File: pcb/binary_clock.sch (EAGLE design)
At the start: 18 parts

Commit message: PCB almost done.
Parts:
- added C1: (no value), rcl:C-EUC0603K
- added R1, R2: (no value), rcl:R-EU_R0603
- added S1: SET, SparkFun-Switches:MOMENTARY-SWITCH-SPST-SMD-5.2-REDUNDANT
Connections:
- new net LED_CK: R1.1, U$1.(OCP)PB1
- new net LED_D: R2.1, U$1.(AREF)PB0
- new net N$31: D17.DO
- new net N$32: U$1.(ADC0)PB5
- new net N$33: U$1.(ADC2)PB4
- new net N$34: D17.CO
- new net N$35: U$1.(ADC3)PB3
- new net N$36: U$1.(ADC1)PB2
- new net N$41: D1.DI, R2.2
- new net N$42: D1.CI, R1.2
- new net SW: S1.1
- net +5V: now also C1.1
- net GND: now also C1.2, S1.2
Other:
- moved on the sheet: D1, D10, D11, D2, D3, D4, D5, D6, D7, D8, D9, U$1

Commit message: Switch connected
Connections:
- removed net N$36: U$1.(ADC1)PB2
- net SW: now also U$1.(ADC1)PB2
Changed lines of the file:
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@@
-</segment>
-</net>
-<net name="N$36" class="0">
-<segment>
-<pinref part="U$1" gate="G$1" pin="(ADC1)PB2"/>
-<wire x1="-12.7" y1="71.12" x2="-10.16" y2="71.12" width="0.1524" layer="91"/>
 </segment>
 </net>
@@
 <label x="17.78" y="60.96" size="0.8128" layer="95" rot="R180" xref="yes"/>
 </segment>
+<segment>
+<pinref part="U$1" gate="G$1" pin="(ADC1)PB2"/>
+<wire x1="-12.7" y1="71.12" x2="-10.16" y2="71.12" width="0.1524" layer="91"/>
+<label x="-10.16" y="71.12" size="0.8128" layer="95" xref="yes"/>
+</segment>
 </net>

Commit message: Routing done.
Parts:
- added R3: (no value), rcl:R-EU_R0603
- added Y1: OSCILLATORSMD-5X3, SparkFun-Clocks:OSCILLATORSMD-5X3
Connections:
- new net N$36: R3.2, S1.1
- net +5V: now also Y1.VCC
- net GND: now also Y1.GND
- net N$35: now also Y1.OUT
- net SW: now also R3.1; no longer S1.1
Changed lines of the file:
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@@
 <?xml version="1.0" encoding="utf-8"?>
 <!DOCTYPE eagle SYSTEM "eagle.dtd">
-<eagle version="7.6.0">
+<eagle version="7.7.0">
 <drawing>
 <settings>
@@
 <layers>
 <layer number="1" name="Top" color="4" fill="1" visible="no" active="no"/>
+<layer number="2" name="Route2" color="1" fill="3" visible="no" active="no"/>
+<layer number="3" name="Route3" color="4" fill="3" visible="no" active="no"/>
+<layer number="4" name="Route4" color="1" fill="4" visible="no" active="no"/>
+<layer number="5" name="Route5" color="4" fill="4" visible="no" active="no"/>
+<layer number="6" name="Route6" color="1" fill="8" visible="no" active="no"/>
+<layer number="7" name="Route7" color="4" fill="8" visible="no" active="no"/>
+<layer number="8" name="Route8" color="1" fill="2" visible="no" active="no"/>
+<layer number="9" name="Route9" color="4" fill="2" visible="no" active="no"/>
+<layer number="10" name="Route10" color="1" fill="7" visible="no" active="no"/>
+<layer number="11" name="Route11" color="4" fill="7" visible="no" active="no"/>
+<layer number="12" name="Route12" color="1" fill="5" visible="no" active="no"/>
+<layer number="13" name="Route13" color="4" fill="5" visible="no" active="no"/>
+<layer number="14" name="Route14" color="1" fill="6" visible="no" active="no"/>
+<layer number="15" name="Route15" color="4" fill="6" visible="no" active="no"/>
 <layer number="16" name="Bottom" color="1" fill="1" visible="no" active="no"/>
 <layer number="17" name="Pads" color="2" fill="1" visible="no" active="no"/>
@@
 <part name="R1" library="rcl" deviceset="R-EU_" device="R0603"/>
 <part name="R2" library="rcl" deviceset="R-EU_" device="R0603"/>
+<part name="Y1" library="SparkFun-Clocks" deviceset="OSCILLATOR" device="SMD-5X3"/>
+<part name="R3" library="rcl" deviceset="R-EU_" device="R0603"/>
 </parts>
 <sheets>
@@
 <instance part="R1" gate="G$1" x="33.02" y="76.2"/>
 <instance part="R2" gate="G$1" x="33.02" y="73.66"/>
+<instance part="Y1" gate="G$1" x="-30.48" y="96.52"/>
+<instance part="R3" gate="G$1" x="12.7" y="60.96"/>
 </instances>
 <busses>
@@
 <label x="-53.34" y="33.02" size="0.8128" layer="95" rot="R180" xref="yes"/>
 </segment>
+<segment>
+<pinref part="Y1" gate="G$1" pin="GND"/>
+<wire x1="-20.32" y1="93.98" x2="-17.78" y2="93.98" width="0.1524" layer="91"/>
+</segment>
 </net>
 <net name="+5V" class="0">
@@
 <wire x1="-53.34" y1="43.18" x2="-53.34" y2="45.72" width="0.1524" layer="91"/>
 <label x="-53.34" y="45.72" size="0.8128" layer="95" rot="R180" xref="yes"/>
+</segment>
+<segment>
+<pinref part="Y1" gate="G$1" pin="VCC"/>
+<wire x1="-40.64" y1="99.06" x2="-43.18" y2="99.06" width="0.1524" layer="91"/>
 </segment>
 </net>
@@
 <segment>
 <pinref part="U$1" gate="G$1" pin="(ADC3)PB3"/>
-<wire x1="-12.7" y1="73.66" x2="-10.16" y2="73.66" width="0.1524" layer="91"/>
+<pinref part="Y1" gate="G$1" pin="OUT"/>
+<wire x1="-20.32" y1="99.06" x2="2.54" y2="99.06" width="0.1524" layer="91"/>
+<wire x1="2.54" y1="99.06" x2="2.54" y2="73.66" width="0.1524" layer="91"/>
+<wire x1="2.54" y1="73.66" x2="-12.7" y2="73.66" width="0.1524" layer="91"/>
 </segment>
 </net>
@@
 <net name="SW" class="0">
 <segment>
-<pinref part="S1" gate="G$1" pin="1"/>
-<wire x1="20.32" y1="60.96" x2="17.78" y2="60.96" width="0.1524" layer="91"/>
-<label x="17.78" y="60.96" size="0.8128" layer="95" rot="R180" xref="yes"/>
-</segment>
-<segment>
 <pinref part="U$1" gate="G$1" pin="(ADC1)PB2"/>
 <wire x1="-12.7" y1="71.12" x2="-10.16" y2="71.12" width="0.1524" layer="91"/>
 <label x="-10.16" y="71.12" size="0.8128" layer="95" xref="yes"/>
 </segment>
-</net>
+<segment>
+<pinref part="R3" gate="G$1" pin="1"/>
+<wire x1="7.62" y1="60.96" x2="5.08" y2="60.96" width="0.1524" layer="91"/>
+<label x="5.08" y="60.96" size="0.8128" layer="95" rot="R180" xref="yes"/>
+</segment>
+</net>
+<net name="N$36" class="0">
+<segment>
+<pinref part="S1" gate="G$1" pin="1"/>
+<pinref part="R3" gate="G$1" pin="2"/>
+<wire x1="17.78" y1="60.96" x2="20.32" y2="60.96" width="0.1524" layer="91"/>
+</segment>
+</net>

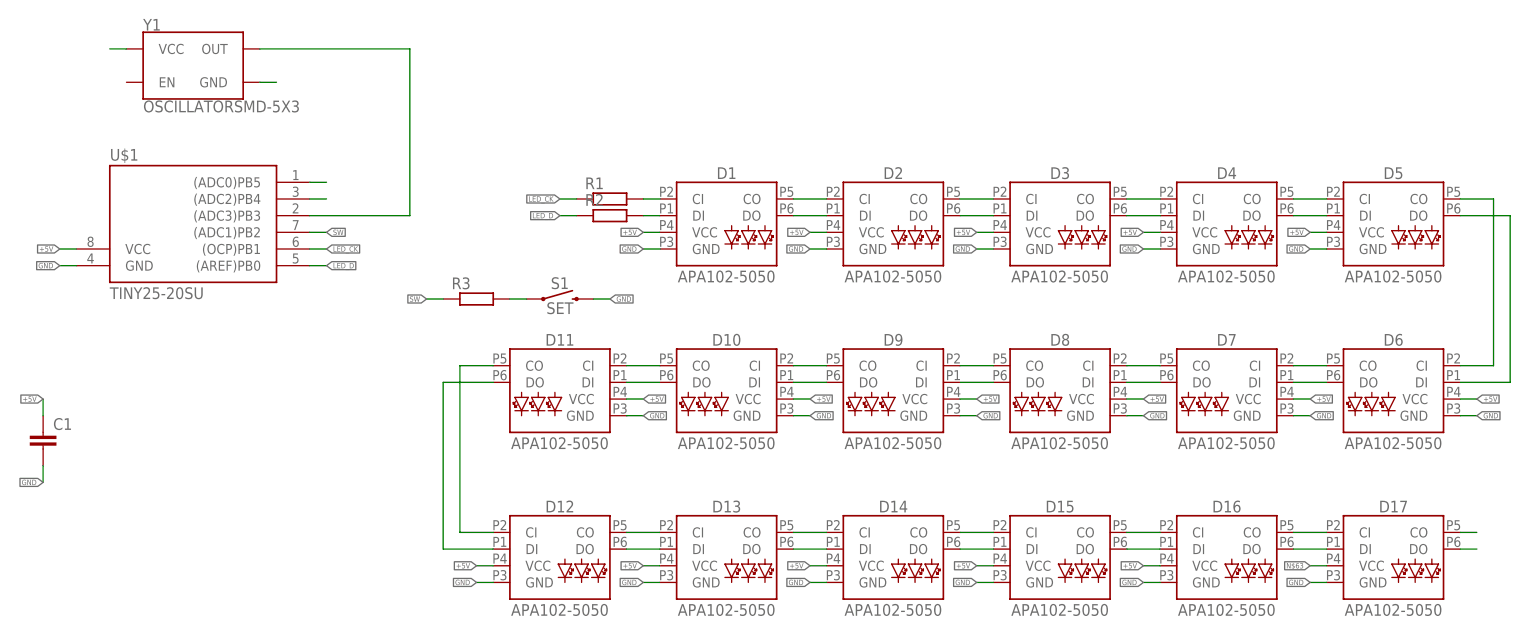
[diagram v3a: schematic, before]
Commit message: Silkscreen and resistor sizes
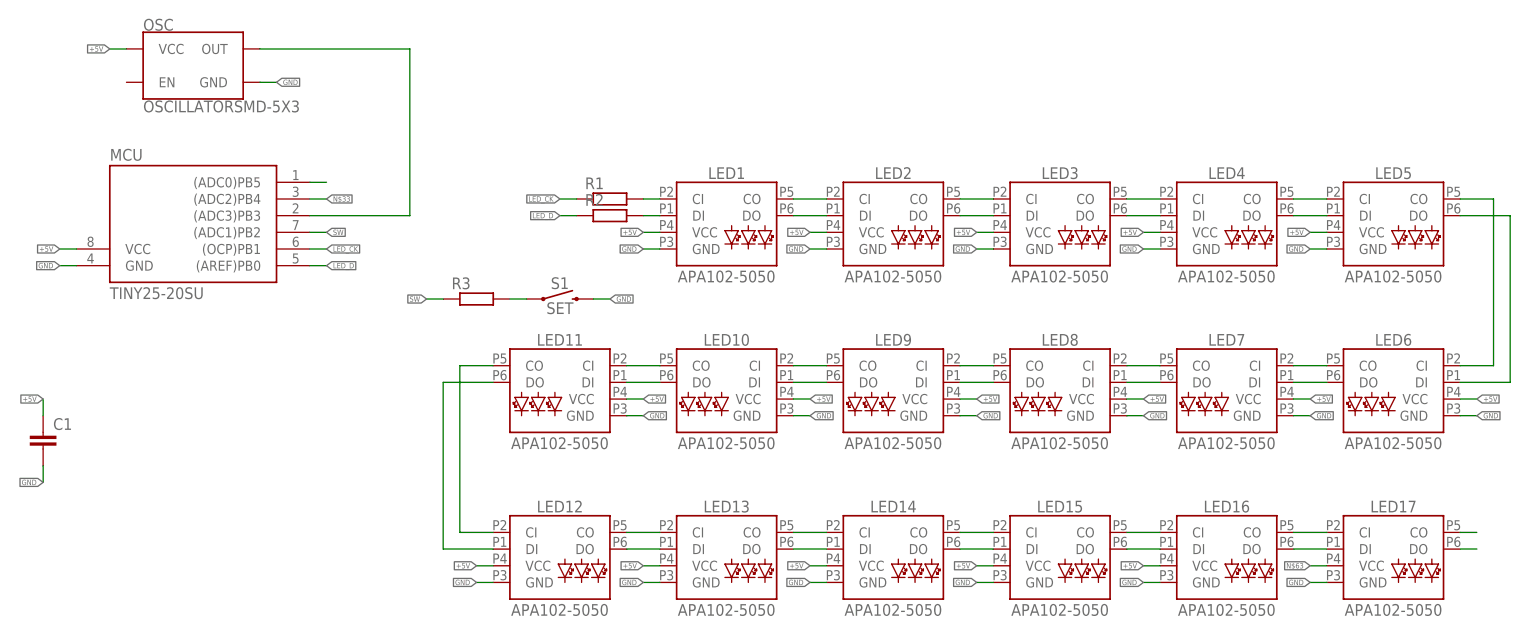
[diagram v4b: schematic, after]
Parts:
- R1, R2, R3: device rcl:R-EU_R0603 -> rcl:R-EU_R1206
- renumbered D1 to LED1, D10 to LED10, D11 to LED11, D12 to LED12, D13 to LED13, D14 to LED14, D15 to LED15, D16 to LED16, D17 to LED17, D2 to LED2, D3 to LED3, D4 to LED4, D5 to LED5, D6 to LED6, D7 to LED7, D8 to LED8, D9 to LED9, U$1 to MCU, Y1 to OSC

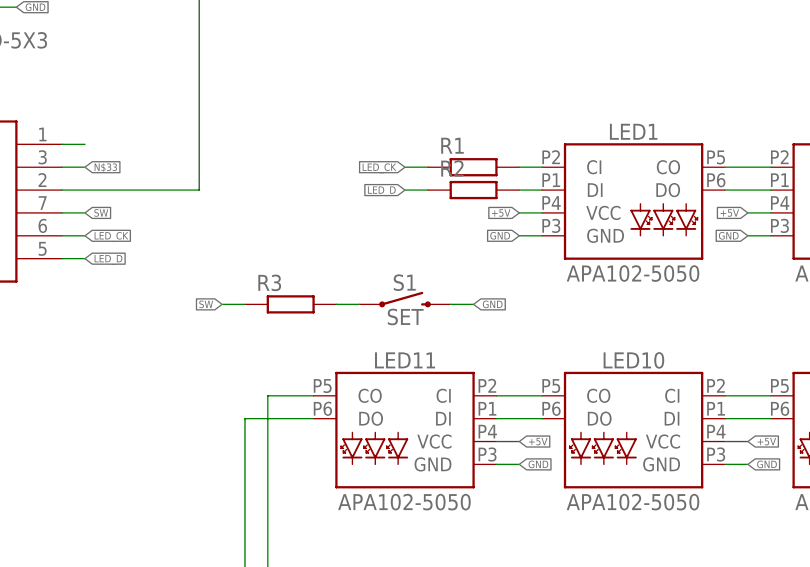
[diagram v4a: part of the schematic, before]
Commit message: Switch renamed
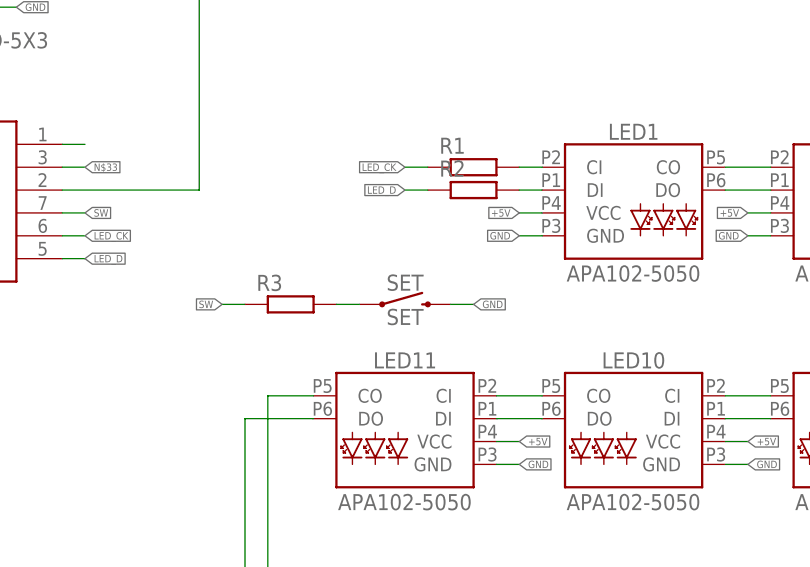
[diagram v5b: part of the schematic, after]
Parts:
- renumbered S1 to SET
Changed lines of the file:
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@@
 <grid distance="0.1" unitdist="inch" unit="inch" style="lines" multiple="1" display="no" altdistance="0.01" altunitdist="inch" altunit="inch"/>
 <layers>
-<layer number="1" name="Top" color="4" fill="1" visible="yes" active="no"/>
-<layer number="2" name="Route2" color="1" fill="3" visible="yes" active="no"/>
-<layer number="3" name="Route3" color="4" fill="3" visible="yes" active="no"/>
-<layer number="4" name="Route4" color="1" fill="4" visible="yes" active="no"/>
-<layer number="5" name="Route5" color="4" fill="4" visible="yes" active="no"/>
-<layer number="6" name="Route6" color="1" fill="8" visible="yes" active="no"/>
-<layer number="7" name="Route7" color="4" fill="8" visible="yes" active="no"/>
-<layer number="8" name="Route8" color="1" fill="2" visible="yes" active="no"/>
-<layer number="9" name="Route9" color="4" fill="2" visible="yes" active="no"/>
-<layer number="10" name="Route10" color="1" fill="7" visible="yes" active="no"/>
-<layer number="11" name="Route11" color="4" fill="7" visible="yes" active="no"/>
-<layer number="12" name="Route12" color="1" fill="5" visible="yes" active="no"/>
-<layer number="13" name="Route13" color="4" fill="5" visible="yes" active="no"/>
-<layer number="14" name="Route14" color="1" fill="6" visible="yes" active="no"/>
-<layer number="15" name="Route15" color="4" fill="6" visible="yes" active="no"/>
-<layer number="16" name="Bottom" color="1" fill="1" visible="yes" active="no"/>
-<layer number="17" name="Pads" color="2" fill="1" visible="yes" active="no"/>
-<layer number="18" name="Vias" color="2" fill="1" visible="yes" active="no"/>
-<layer number="19" name="Unrouted" color="6" fill="1" visible="yes" active="no"/>
-<layer number="20" name="Dimension" color="15" fill="1" visible="yes" active="no"/>
-<layer number="21" name="tPlace" color="7" fill="1" visible="yes" active="no"/>
-<layer number="22" name="bPlace" color="7" fill="1" visible="yes" active="no"/>
-<layer number="23" name="tOrigins" color="15" fill="1" visible="yes" active="no"/>
-<layer number="24" name="bOrigins" color="15" fill="1" visible="yes" active="no"/>
-<layer number="25" name="tNames" color="7" fill="1" visible="yes" active="no"/>
-<layer number="26" name="bNames" color="7" fill="1" visible="yes" active="no"/>
-<layer number="27" name="tValues" color="7" fill="1" visible="yes" active="no"/>
-<layer number="28" name="bValues" color="7" fill="1" visible="yes" active="no"/>
+<layer number="1" name="Top" color="4" fill="1" visible="no" active="no"/>
+<layer number="2" name="Route2" color="1" fill="3" visible="no" active="no"/>
+<layer number="3" name="Route3" color="4" fill="3" visible="no" active="no"/>
+<layer number="4" name="Route4" color="1" fill="4" visible="no" active="no"/>
+<layer number="5" name="Route5" color="4" fill="4" visible="no" active="no"/>
+<layer number="6" name="Route6" color="1" fill="8" visible="no" active="no"/>
+<layer number="7" name="Route7" color="4" fill="8" visible="no" active="no"/>
+<layer number="8" name="Route8" color="1" fill="2" visible="no" active="no"/>
+<layer number="9" name="Route9" color="4" fill="2" visible="no" active="no"/>
+<layer number="10" name="Route10" color="1" fill="7" visible="no" active="no"/>
+<layer number="11" name="Route11" color="4" fill="7" visible="no" active="no"/>
+<layer number="12" name="Route12" color="1" fill="5" visible="no" active="no"/>
+<layer number="13" name="Route13" color="4" fill="5" visible="no" active="no"/>
+<layer number="14" name="Route14" color="1" fill="6" visible="no" active="no"/>
+<layer number="15" name="Route15" color="4" fill="6" visible="no" active="no"/>
+<layer number="16" name="Bottom" color="1" fill="1" visible="no" active="no"/>
+<layer number="17" name="Pads" color="2" fill="1" visible="no" active="no"/>
+<layer number="18" name="Vias" color="2" fill="1" visible="no" active="no"/>
+<layer number="19" name="Unrouted" color="6" fill="1" visible="no" active="no"/>
+<layer number="20" name="Dimension" color="15" fill="1" visible="no" active="no"/>
+<layer number="21" name="tPlace" color="7" fill="1" visible="no" active="no"/>
+<layer number="22" name="bPlace" color="7" fill="1" visible="no" active="no"/>
+<layer number="23" name="tOrigins" color="15" fill="1" visible="no" active="no"/>
+<layer number="24" name="bOrigins" color="15" fill="1" visible="no" active="no"/>
+<layer number="25" name="tNames" color="7" fill="1" visible="no" active="no"/>
+<layer number="26" name="bNames" color="7" fill="1" visible="no" active="no"/>
+<layer number="27" name="tValues" color="7" fill="1" visible="no" active="no"/>
+<layer number="28" name="bValues" color="7" fill="1" visible="no" active="no"/>
 <layer number="29" name="tStop" color="7" fill="3" visible="no" active="no"/>
 <layer number="30" name="bStop" color="7" fill="6" visible="no" active="no"/>
@@
 <layer number="35" name="tGlue" color="7" fill="4" visible="no" active="no"/>
 <layer number="36" name="bGlue" color="7" fill="5" visible="no" active="no"/>
-<layer number="37" name="tTest" color="7" fill="1" visible="yes" active="no"/>
-<layer number="38" name="bTest" color="7" fill="1" visible="yes" active="no"/>
+<layer number="37" name="tTest" color="7" fill="1" visible="no" active="no"/>
+<layer number="38" name="bTest" color="7" fill="1" visible="no" active="no"/>
 <layer number="39" name="tKeepout" color="4" fill="11" visible="no" active="no"/>
 <layer number="40" name="bKeepout" color="1" fill="11" visible="no" active="no"/>
@@
 <layer number="44" name="Drills" color="7" fill="1" visible="no" active="no"/>
 <layer number="45" name="Holes" color="7" fill="1" visible="no" active="no"/>
-<layer number="46" name="Milling" color="3" fill="1" visible="yes" active="no"/>
-<layer number="47" name="Measures" color="7" fill="1" visible="yes" active="no"/>
-<layer number="48" name="Document" color="7" fill="1" visible="yes" active="no"/>
-<layer number="49" name="Reference" color="7" fill="1" visible="yes" active="no"/>
-<layer number="50" name="dxf" color="7" fill="1" visible="yes" active="no"/>
-<layer number="51" name="tDocu" color="7" fill="1" visible="yes" active="no"/>
-<layer number="52" name="bDocu" color="7" fill="1" visible="yes" active="no"/>
-<layer number="53" name="tGND_GNDA" color="7" fill="9" visible="yes" active="no"/>
-<layer number="54" name="bGND_GNDA" color="1" fill="9" visible="yes" active="no"/>
-<layer number="56" name="wert" color="7" fill="1" visible="yes" active="no"/>
-<layer number="57" name="tCAD" color="7" fill="1" visible="yes" active="no"/>
-<layer number="59" name="tCarbon" color="7" fill="1" visible="yes" active="no"/>
-<layer number="60" name="bCarbon" color="7" fill="1" visible="yes" active="no"/>
+<layer number="46" name="Milling" color="3" fill="1" visible="no" active="no"/>
+<layer number="47" name="Measures" color="7" fill="1" visible="no" active="no"/>
+<layer number="48" name="Document" color="7" fill="1" visible="no" active="no"/>
+<layer number="49" name="Reference" color="7" fill="1" visible="no" active="no"/>
+<layer number="50" name="dxf" color="7" fill="1" visible="no" active="no"/>
+<layer number="51" name="tDocu" color="7" fill="1" visible="no" active="no"/>
+<layer number="52" name="bDocu" color="7" fill="1" visible="no" active="no"/>
+<layer number="53" name="tGND_GNDA" color="7" fill="9" visible="no" active="no"/>
+<layer number="54" name="bGND_GNDA" color="1" fill="9" visible="no" active="no"/>
+<layer number="56" name="wert" color="7" fill="1" visible="no" active="no"/>
+<layer number="57" name="tCAD" color="7" fill="1" visible="no" active="no"/>
+<layer number="59" name="tCarbon" color="7" fill="1" visible="no" active="no"/>
+<layer number="60" name="bCarbon" color="7" fill="1" visible="no" active="no"/>
 <layer number="90" name="Modules" color="5" fill="1" visible="yes" active="yes"/>
 <layer number="91" name="Nets" color="2" fill="1" visible="yes" active="yes"/>
@@
 <part name="LED17" library="SparkFun-LED" deviceset="APA102" device="-5050"/>
 <part name="MCU" library="avr-4" deviceset="TINY25" device="-20SU"/>
-<part name="S1" library="SparkFun-Switches" deviceset="MOMENTARY-SWITCH-SPST" device="-SMD-5.2-REDUNDANT" value="SET"/>
+<part name="SET" library="SparkFun-Switches" deviceset="MOMENTARY-SWITCH-SPST" device="-SMD-5.2-REDUNDANT" value="SET"/>
 <part name="C1" library="rcl" deviceset="C-EU" device="C0603K"/>
 <part name="R1" library="rcl" deviceset="R-EU_" device="R1206"/>
@@
 <instance part="LED17" gate="G$1" x="152.4" y="22.86"/>
 <instance part="MCU" gate="G$1" x="-30.48" y="71.12"/>
-<instance part="S1" gate="G$1" x="25.4" y="60.96"/>
+<instance part="SET" gate="G$1" x="25.4" y="60.96"/>
 <instance part="C1" gate="G$1" x="-53.34" y="40.64"/>
 <instance part="R1" gate="G$1" x="33.02" y="76.2"/>
@@
 </segment>
 <segment>
-<pinref part="S1" gate="G$1" pin="2"/>
+<pinref part="SET" gate="G$1" pin="2"/>
 <wire x1="30.48" y1="60.96" x2="33.02" y2="60.96" width="0.1524" layer="91"/>
 <label x="33.02" y="60.96" size="0.8128" layer="95" xref="yes"/>
@@
 <net name="N$36" class="0">
 <segment>
-<pinref part="S1" gate="G$1" pin="1"/>
+<pinref part="SET" gate="G$1" pin="1"/>
 <pinref part="R3" gate="G$1" pin="2"/>
 <wire x1="17.78" y1="60.96" x2="20.32" y2="60.96" width="0.1524" layer="91"/>
